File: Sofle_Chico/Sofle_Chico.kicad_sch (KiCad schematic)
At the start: 120 parts, among them J1 Conn_01x05, J2 MJ-4PP-9, J3 Conn_01x04, J4 Conn_01x04, J5 Conn_01x05, J6 Conn_01x05, J7 Conn_01x04, Q1 DMG2305UX, SW1 SW_PUSH, SW10 SW_PUSH, SW11 SW_PUSH, SW12 SW_PUSH, SW13 SW_PUSH, SW14 SW_PUSH, SW15 SW_PUSH, SW16 SW_PUSH, SW17 SW_PUSH, SW18 SW_PUSH, SW19 SW_PUSH, SW2 SW_PUSH, SW20 SW_PUSH, SW21 SW_PUSH, SW22 SW_PUSH, SW23 SW_PUSH, SW24 SW_PUSH, SW25 Rotary_Encoder_Switch-Device, SW26 SW_PUSH, SW27 SW_PUSH, SW28 SW_PUSH, SW29 SW_PUSH, SW3 SW_PUSH, SW30 SW_PUSH, SW4 SW_PUSH, SW5 SW_PUSH, SW6 SW_PUSH, SW7 SW_PUSH, SW8 SW_PUSH, SW9 SW_PUSH, U1 SN74AHCT1G125, U2 Pico

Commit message: commit/push again to synch between PCs
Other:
- note added: "D31 is not required for official RPI Pico boards that have an onboard Zener Diode. Refer to Sofle-Pico build guide and your exact RPI Module SCH +VDC is variable! User MUST know/verify their VSYS pin voltage! Read RPI Pico datasheet Chapter 4.5-4.6 +VDC≈4.9-5.0V w/ USB Power +VDC≈4.7-4.9V w/ TRRS Power +VDC≈ VBATT if using a battery"
- note removed: "Refer to Sofle Pico build guide and your SPECIFIC RPI Module SCH before installing D31 +VDC is variable! User MUST know/verify their VSYS pin voltage! Read RPI Pico datasheet Chapter 4.5-4.6 +VDC≈4.9-5.0V w/ USB Power +VDC≈4.7-4.9V w/ TRRS Power +VDC≈ VBATT if using a battery"
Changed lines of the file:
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@@
     (effects (font (size 1.27 1.27)) (justify left bottom))
   )
-  (text "Refer to Sofle Pico build guide \nand your SPECIFIC RPI Module SCH \nbefore installing D31\n\n+VDC is variable! User MUST\nknow/verify their VSYS pin voltage!\nRead RPI Pico datasheet Chapter 4.5-4.6\n+VDC≈4.9-5.0V w/ USB Power\n+VDC≈4.7-4.9V w/ TRRS Power\n+VDC≈ VBATT if using a battery"
-    (at 82.55 34.29 0)
+  (text "D31 is not required for official RPI Pico \nboards that have an onboard Zener Diode.\nRefer to Sofle-Pico build guide \nand your exact RPI Module SCH \n\n+VDC is variable! User MUST\nknow/verify their VSYS pin voltage!\nRead RPI Pico datasheet Chapter 4.5-4.6\n+VDC≈4.9-5.0V w/ USB Power\n+VDC≈4.7-4.9V w/ TRRS Power\n+VDC≈ VBATT if using a battery"
+    (at 82.55 38.1 0)
     (effects (font (size 1.27 1.27)) (justify left bottom))
   )

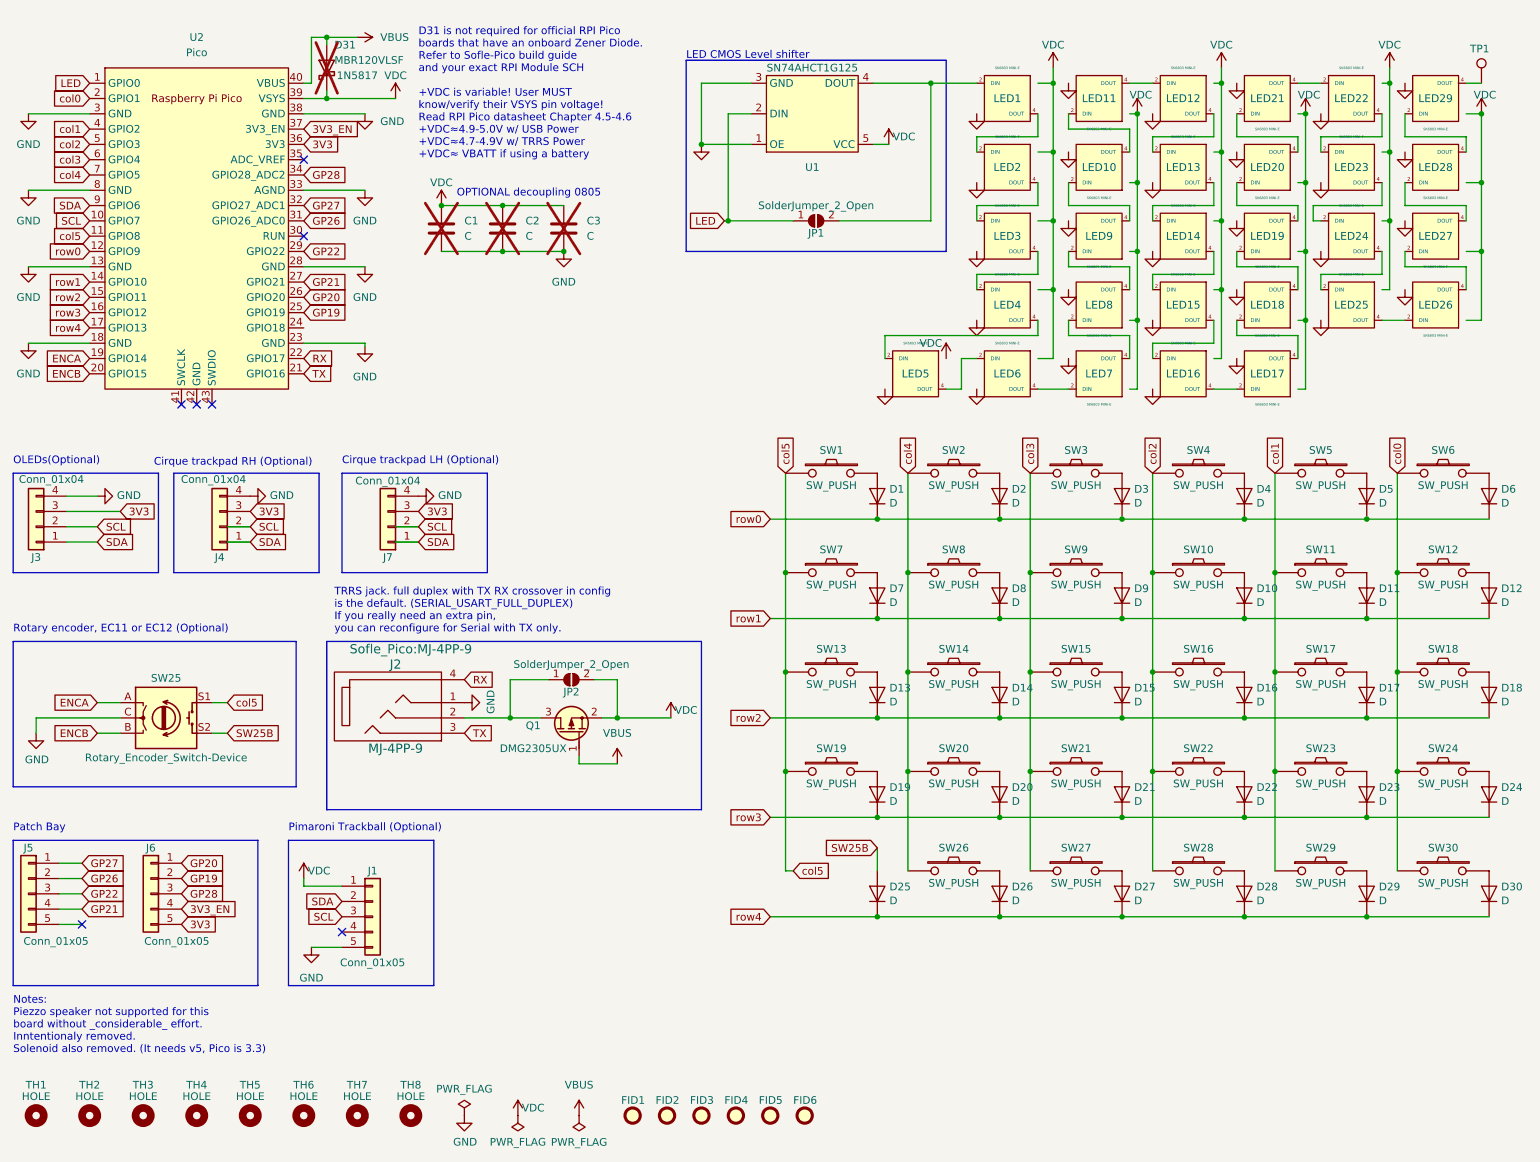
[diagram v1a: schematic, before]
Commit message: Fixing POS files to be minimal set and figuring out how coordinates/position files correlate
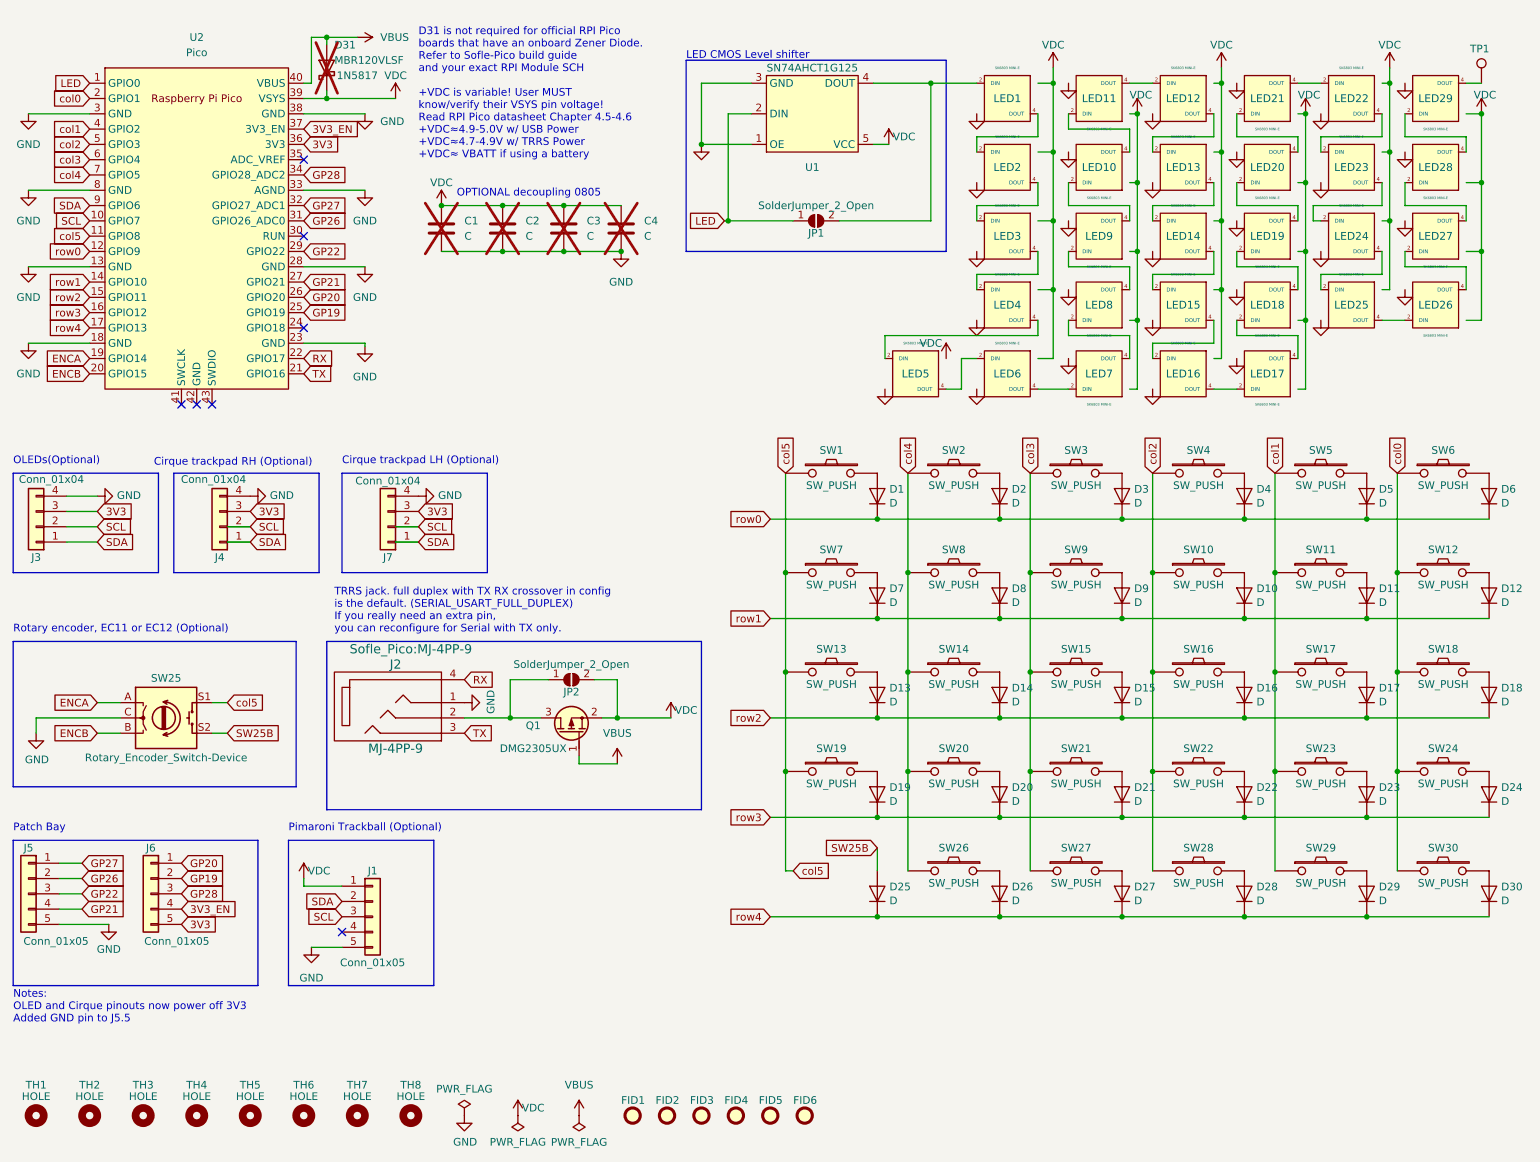
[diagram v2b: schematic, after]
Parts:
- added C4: C, Capacitor_SMD:C_0805_2012Metric_Pad1.18x1.45mm_HandSolder, symbol Device:C
- C1, C2, C3, J1, J3, J4, J6, J7: now left out of the parts list
- J5: footprint Sofle_Pico:PinHeader_1x05_P2.54mm_Vertical_one-dead -> Sofle_Pico:PinHeader_1x05_P2.54mm_Vertical; now left out of the parts list
- TH1, TH2, TH3, TH4, TH6, TH7, TH8: footprint (none) -> Sofle_Pico:keyplate_hole_M2_standoff_passthrough
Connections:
- net GND: now also J5.5 (Pin_5), C4.2
- net VDC: now also C4.1
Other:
- note added: "Notes: OLED and Cirque pinouts now power off 3V3 Added GND pin to J5.5"
- note removed: "Notes: Piezzo speaker not supported for this board without _considerable_ effort. Inntentionaly removed. Solenoid also removed. (It needs v5, Pico is 3.3)"
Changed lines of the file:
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@@
   (junction (at 219.71 130.81) (diameter 0) (color 0 0 0 0)
   )
+  (junction (at 116.205 53.34) (diameter 0) (color 0 0 0 0)
+  )
   (junction (at 143.51 106.68) (diameter 0) (color 0 0 0 0)
   )
@@
   (junction (at 187.96 36.83) (diameter 0) (color 0 0 0 0)
   )
+  (junction (at 106.68 45.72) (diameter 0) (color 0 0 0 0)
+  )
   (junction (at 199.39 114.3) (diameter 0) (color 0 0 0 0)
   )
@@
   )
   (no_connect (at 63.5 50.8))
-  (no_connect (at 26.67 165.1))
   (no_connect (at 63.5 38.1))
   (no_connect (at 45.72 78.74))
+  (no_connect (at 63.5 66.04))
   (no_connect (at 43.18 78.74))
   (no_connect (at 69.85 166.37))
@@
     (stroke (width 0) (type default))
   )
-  (wire (pts (xy 22.86 165.1) (xy 26.67 165.1))
+  (wire (pts (xy 22.86 165.1) (xy 31.115 165.1))
     (stroke (width 0) (type default))
   )
@@
     (stroke (width 0) (type default))
   )
+  (wire (pts (xy 106.68 45.72) (xy 116.205 45.72))
+    (stroke (width 0) (type default))
+  )
   (wire (pts (xy 243.84 22.86) (xy 243.84 25.4))
     (stroke (width 0) (type default))
@@
     (stroke (width 0) (type default))
   )
+  (wire (pts (xy 106.68 53.34) (xy 116.205 53.34))
+    (stroke (width 0) (type default))
+  )
   (wire (pts (xy 97.79 130.81) (xy 102.87 130.81))
     (stroke (width 0) (type default))
@@
     (stroke (width 0) (type default))
   )
-  (wire (pts (xy 24.13 96.52) (xy 33.02 96.52))
+  (wire (pts (xy 24.13 96.52) (xy 29.21 96.52))
     (stroke (width 0) (type default))
   )
@@
     (effects (font (size 1.27 1.27)) (justify left bottom))
   )
-  (text "Notes:\nPiezzo speaker not supported for this \nboard without _considerable_ effort. \nInntentionaly removed.\nSolenoid also removed. (It needs v5, Pico is 3.3)"
-    (at 15.24 186.69 0)
-    (effects (font (size 1.27 1.27)) (justify left bottom))
+  (text "Notes:\nOLED and Cirque pinouts now power off 3V3 \nAdded GND pin to J5.5  "
+    (at 15.24 181.61 0)
+    (effects (font (size 1.27 1.27)) (justify left bottom) (href "#1"))
   )
   (global_label "SDA" (shape input) (at 29.21 101.6 0)
@@
     )
   )
-  (global_label "3V3" (shape input) (at 33.02 96.52 0) (fields_autoplaced)
+  (global_label "3V3" (shape input) (at 29.21 96.52 0) (fields_autoplaced)
     (effects (font (size 1.27 1.27)) (justify left))
-    (property "Intersheetrefs" "${INTERSHEET_REFS}" (at 38.7792 96.52 0)
+    (property "Intersheetrefs" "${INTERSHEET_REFS}" (at 34.9692 96.52 0)
       (effects (font (size 1.27 1.27)) (justify left) hide)
     )
@@
       (effects (font (size 1.27 1.27)))
     )
-    (property "Footprint" "" (at 19.05 196.85 0)
+    (property "Footprint" "Sofle_Pico:keyplate_hole_M2_standoff_passthrough" (at 19.05 196.85 0)
       (effects (font (size 1.27 1.27)) hide)
     )
@@
       (effects (font (size 1.27 1.27)))
     )
-    (property "Footprint" "" (at 27.94 196.85 0)
+    (property "Footprint" "Sofle_Pico:keyplate_hole_M2_standoff_passthrough" (at 27.94 196.85 0)
       (effects (font (size 1.27 1.27)) hide)
     )
@@
       (effects (font (size 1.27 1.27)))
     )
-    (property "Footprint" "" (at 45.72 196.85 0)
+    (property "Footprint" "Sofle_Pico:keyplate_hole_M2_standoff_passthrough" (at 45.72 196.85 0)
       (effects (font (size 1.27 1.27)) hide)
     )
@@
       (effects (font (size 1.27 1.27)))
     )
-    (property "Footprint" "" (at 63.5 196.85 0)
+    (property "Footprint" "Sofle_Pico:keyplate_hole_M2_standoff_passthrough" (at 63.5 196.85 0)
       (effects (font (size 1.27 1.27)) hide)
     )
@@
       (effects (font (size 1.27 1.27)))
     )
-    (property "Footprint" "" (at 72.39 196.85 0)
+    (property "Footprint" "Sofle_Pico:keyplate_hole_M2_standoff_passthrough" (at 72.39 196.85 0)
       (effects (font (size 1.27 1.27)) hide)
     )
@@
       (effects (font (size 1.27 1.27)))
     )
-    (property "Footprint" "" (at 36.83 196.85 0)
+    (property "Footprint" "Sofle_Pico:keyplate_hole_M2_standoff_passthrough" (at 36.83 196.85 0)
       (effects (font (size 1.27 1.27)) hide)
     )
@@
   )
   (symbol (lib_id "Connector_Generic:Conn_01x04") (at 19.05 99.06 180) (unit 1)
-    (in_bom yes) (on_board yes) (dnp no)
+    (in_bom no) (on_board yes) (dnp no)
     (property "Reference" "J3" (at 19.05 104.14 0)
       (effects (font (size 1.27 1.27)))
@@
   )
   (symbol (lib_id "Sofle_Pico:Conn_01x04") (at 49.53 99.06 180) (unit 1)
-    (in_bom yes) (on_board yes) (dnp no)
+    (in_bom no) (on_board yes) (dnp no)
     (property "Reference" "J4" (at 49.53 104.14 0)
       (effects (font (size 1.27 1.27)))
@@
     )
   )
+  (symbol (lib_id "Device:C") (at 116.205 49.53 0) (unit 1)
+    (in_bom no) (on_board yes) (dnp yes)
+    (property "Reference" "C4" (at 120.015 48.26 0)
+      (effects (font (size 1.27 1.27)) (justify left))
+    )
+    (property "Value" "C" (at 120.015 50.8 0)
+      (effects (font (size 1.27 1.27)) (justify left))
+    )
+    (property "Footprint" "Capacitor_SMD:C_0805_2012Metric_Pad1.18x1.45mm_HandSolder" (at 117.1702 53.34 0)
+      (effects (font (size 1.27 1.27)) hide)
+    )
+    (property "Datasheet" "~" (at 116.205 49.53 0)
+      (effects (font (size 1.27 1.27)) hide)
+    )
+    (pin "2")
+    (pin "1")
+    (instances
+      (project "Sofle_Chico"
+        (path "/06057b3a-55ab-4f4e-913e-2aeec5ff3587"
+          (reference "C4") (unit 1)
+        )
+      )
+    )
+  )
   (symbol (lib_name "GND_1") (lib_id "power:GND") (at 175.26 41.91 0) (unit 1)
     (in_bom yes) (on_board yes) (dnp no)
@@
   )
   (symbol (lib_id "Sofle_Pico:Conn_01x05") (at 74.93 163.83 0) (unit 1)
-    (in_bom yes) (on_board yes) (dnp no)
+    (in_bom no) (on_board yes) (dnp no)
     (property "Reference" "J1" (at 74.93 156.21 0)
       (effects (font (size 1.27 1.27)))
@@
   )
   (symbol (lib_id "Device:C") (at 106.68 49.53 0) (unit 1)
-    (in_bom yes) (on_board yes) (dnp yes)
+    (in_bom no) (on_board yes) (dnp yes)
     (property "Reference" "C3" (at 110.49 48.26 0)
       (effects (font (size 1.27 1.27)) (justify left))
@@
     )
   )
+  (symbol (lib_id "power:GND") (at 31.115 165.1 0) (unit 1)
+    (in_bom yes) (on_board yes) (dnp no) (fields_autoplaced)
+    (property "Reference" "#PWR010" (at 31.115 171.45 0)
+      (effects (font (size 1.27 1.27)) hide)
+    )
+    (property "Value" "GND" (at 31.115 169.2331 0)
+      (effects (font (size 1.27 1.27)))
+    )
+    (property "Footprint" "" (at 31.115 165.1 0)
+      (effects (font (size 1.27 1.27)) hide)
+    )
+    (property "Datasheet" "" (at 31.115 165.1 0)
+      (effects (font (size 1.27 1.27)) hide)
+    )
+    (pin "1")
+    (instances
+      (project "Sofle_Chico"
+        (path "/06057b3a-55ab-4f4e-913e-2aeec5ff3587"
+          (reference "#PWR010") (unit 1)
+        )
+      )
+    )
+  )
   (symbol (lib_name "VDC_1") (lib_id "power:VDC") (at 187.96 22.86 0) (unit 1)
     (in_bom yes) (on_board yes) (dnp no)
@@
   )
   (symbol (lib_id "Sofle_Pico:Conn_01x04") (at 77.47 99.06 180) (unit 1)
-    (in_bom yes) (on_board yes) (dnp no)
+    (in_bom no) (on_board yes) (dnp no)
     (property "Reference" "J7" (at 77.47 104.14 0)
       (effects (font (size 1.27 1.27)))
@@
     )
   )
-  (symbol (lib_name "GND_5") (lib_id "power:GND") (at 106.68 53.34 0) (unit 1)
+  (symbol (lib_name "GND_5") (lib_id "power:GND") (at 116.205 53.34 0) (unit 1)
     (in_bom yes) (on_board yes) (dnp no) (fields_autoplaced)
-    (property "Reference" "#PWR015" (at 106.68 59.69 0)
+    (property "Reference" "#PWR015" (at 116.205 59.69 0)
       (effects (font (size 1.27 1.27)) hide)
     )
-    (property "Value" "GND" (at 106.68 58.42 0)
+    (property "Value" "GND" (at 116.205 58.42 0)
       (effects (font (size 1.27 1.27)))
     )
-    (property "Footprint" "" (at 106.68 53.34 0)
+    (property "Footprint" "" (at 116.205 53.34 0)
       (effects (font (size 1.27 1.27)) hide)
     )
-    (property "Datasheet" "" (at 106.68 53.34 0)
+    (property "Datasheet" "" (at 116.205 53.34 0)
       (effects (font (size 1.27 1.27)) hide)
     )
@@
       (effects (font (size 1.27 1.27)))
     )
-    (property "Footprint" "" (at 81.28 196.85 0)
+    (property "Footprint" "Sofle_Pico:keyplate_hole_M2_standoff_passthrough" (at 81.28 196.85 0)
       (effects (font (size 1.27 1.27)) hide)
     )
@@
   )
   (symbol (lib_id "Sofle_Pico:Conn_01x05") (at 38.1 160.02 0) (mirror y) (unit 1)
-    (in_bom yes) (on_board yes) (dnp no)
+    (in_bom no) (on_board yes) (dnp no)
     (property "Reference" "J6" (at 38.1 152.4 0)
       (effects (font (size 1.27 1.27)))
@@
   )
   (symbol (lib_id "Device:C") (at 86.36 49.53 0) (unit 1)
-    (in_bom yes) (on_board yes) (dnp yes) (fields_autoplaced)
+    (in_bom no) (on_board yes) (dnp yes) (fields_autoplaced)
     (property "Reference" "C1" (at 90.17 48.26 0)
       (effects (font (size 1.27 1.27)) (justify left))
@@
   )
   (symbol (lib_id "Sofle_Pico:Conn_01x05") (at 17.78 160.02 0) (mirror y) (unit 1)
-    (in_bom yes) (on_board yes) (dnp no)
+    (in_bom no) (on_board yes) (dnp no)
     (property "Reference" "J5" (at 17.78 152.4 0)
       (effects (font (size 1.27 1.27)))
@@
       (effects (font (size 1.27 1.27)))
     )
-    (property "Footprint" "Sofle_Pico:PinHeader_1x05_P2.54mm_Vertical_one-dead" (at 17.78 160.02 0)
+    (property "Footprint" "Sofle_Pico:PinHeader_1x05_P2.54mm_Vertical" (at 17.78 160.02 0)
       (effects (font (size 1.27 1.27)) hide)
     )
@@
   )
   (symbol (lib_id "Device:C") (at 96.52 49.53 0) (unit 1)
-    (in_bom yes) (on_board yes) (dnp yes) (fields_autoplaced)
+    (in_bom no) (on_board yes) (dnp yes) (fields_autoplaced)
     (property "Reference" "C2" (at 100.33 48.26 0)
       (effects (font (size 1.27 1.27)) (justify left))
